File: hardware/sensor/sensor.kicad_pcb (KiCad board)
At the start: 2 copper layers, 64 x 32 mm, 35 parts, among them IC1 ATTINY202-SSN, IC2 Si4012-C1001GTR, IC3 TPS3839L30DBZR, J1 M20-9770342

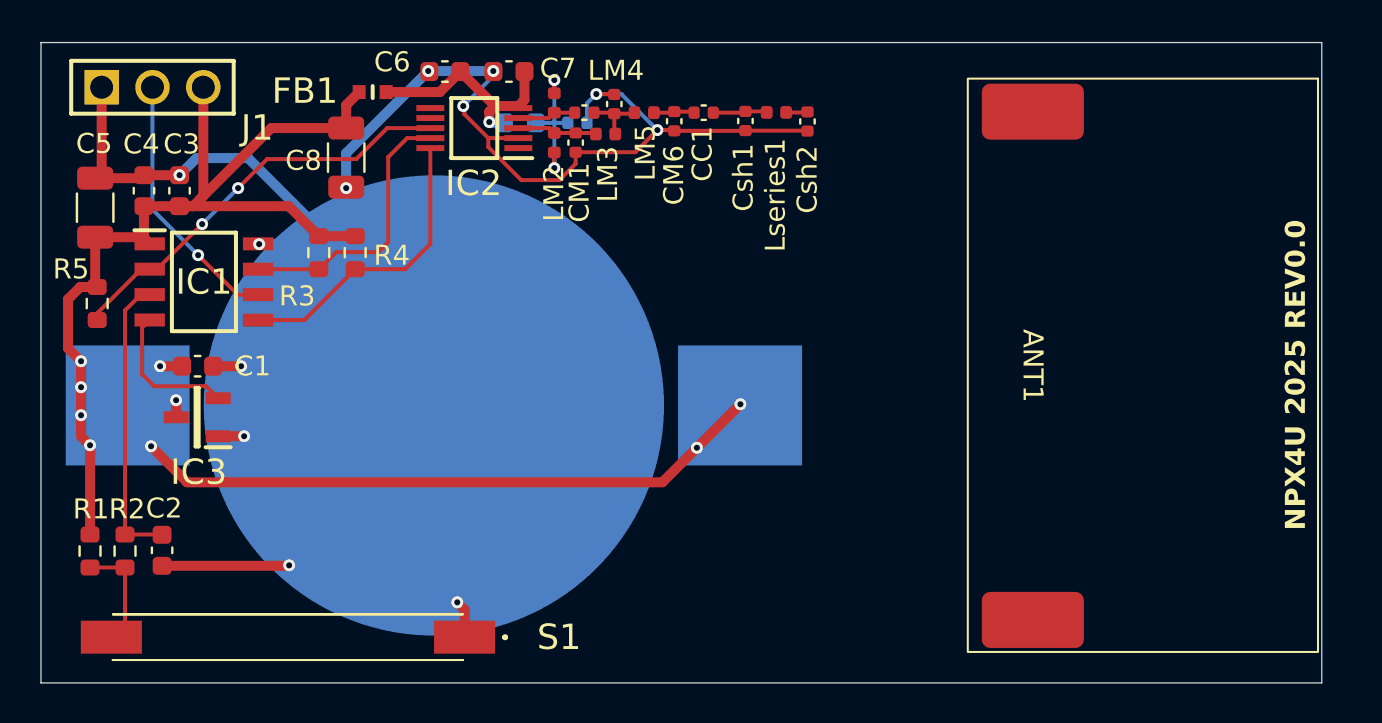
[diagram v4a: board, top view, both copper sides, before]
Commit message: EG-22 All connections, including antenna path and ground planes. Only vias are missing between groud planes.
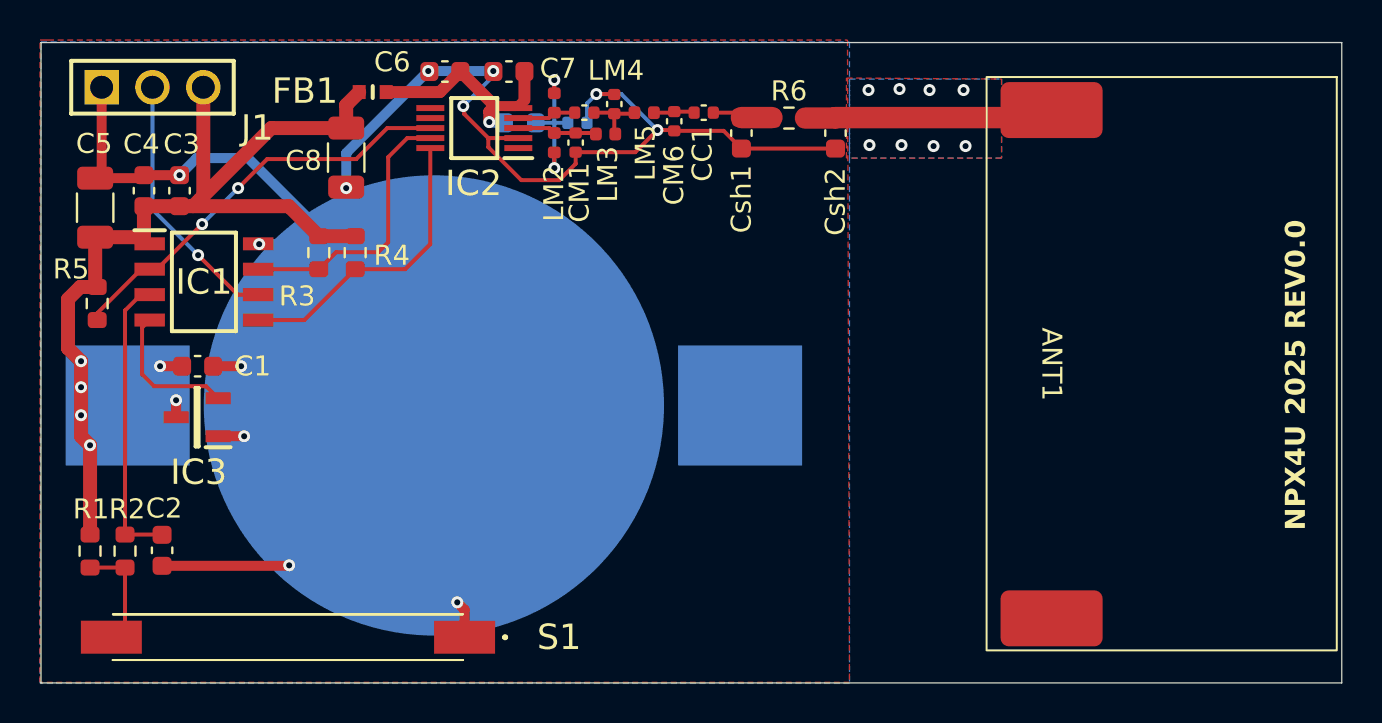
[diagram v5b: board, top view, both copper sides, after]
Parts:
- removed Lseries1: 15nH, Inductor_SMD:L_0402_1005Metric
- added R6: 0, Resistor_SMD:R_0603_1608Metric, F.Cu at (215.1, 130.9)
- Csh1, Csh2: value 0pF -> NC; footprint Capacitor_SMD:C_0402_1005Metric -> Capacitor_SMD:C_0603_1608Metric
- moved Csh2 1.52 mm to (217.4, 131.7)
- moved ANT1 0.94 mm to (228.2, 143.2)
- moved Csh1 0.64 mm to (212.7, 131.7)
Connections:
- H1 pad 1: 3.0V -> unconnected-(H1-+_1-Pad1)
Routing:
- net 3.0V: track 84.1 -> 52.2 mm, vias 9 -> 6
- net Net-(ANT1-Pad1): track 1.09 -> 12.5 mm
- net GND: track 115.9 -> 117.7 mm, vias 12 -> 20
- added copper zone on B.Cu, net GND
- added copper zone on F.Cu, net GND
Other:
- board size 64 x 32 mm -> 65 x 32 mm

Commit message: EG-22 All vias placed.
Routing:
- net GND: vias 20 -> 123

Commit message: EG-29 MCU changed on schematic.
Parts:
- removed IC1: ATTINY202-SSN, MyParts:SOIC127P600X175-8N
- added IC4: STM8L001J3M3, MyParts:SOIC127P600X175-8N, F.Cu at (166.7, 138.9)
- moved IC3 17.3 mm to (168.3, 148.0)
- moved C1 17.3 mm to (168.3, 145.4)
- moved R3 7.47 mm to (198.9, 139.0)
- moved R4 7.47 mm to (200.8, 138.9)
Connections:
- J1 pad 2: UPDI -> SWIM
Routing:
- net SDN: track 21.3 -> 0.00 mm, vias 2 -> 0
- net SDA: track 15.0 -> 0.00 mm
- net GND: track 117.7 -> 102.8 mm, vias 123 -> 117
- net SCL: track 14.0 -> 0.00 mm
- net WND: track 15.1 -> 1.91 mm
- net UPDI: track 13.2 -> 0.00 mm, vias 1 -> 0
- net 3.0V: track 52.2 -> 40.9 mm, vias 6 -> 4
- net LOW_BAT: track 7.16 -> 0.00 mm

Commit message: EG-29 MCU changed on PCB and antenna distance fixed.
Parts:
- moved IC1 18.1 mm to (184.8, 139.9)
- moved C1 17.2 mm to (185.5, 144.7)
- moved IC3 17.2 mm to (185.5, 147.2)
- moved R4 10.1 mm to (190.7, 137.6)
- moved R3 10.1 mm to (188.9, 137.6)
- moved ANT1 2.90 mm to (231.1, 143.2)
- renumbered IC4 to IC1
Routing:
- net GND: track 102.8 -> 133.1 mm, vias 117 -> 126
- net SDN: track 0.00 -> 24.6 mm, vias 0 -> 2
- net SDA: track 0.00 -> 21.4 mm
- net SCL: track 0.00 -> 18.6 mm
- net WND: track 1.91 -> 15.9 mm
- net SWIM: track 0.00 -> 10.7 mm, vias 0 -> 1
- net 3.0V: track 40.9 -> 48.3 mm, vias 4 -> 6
- net LOW_BAT: track 0.00 -> 7.01 mm
- net Net-(ANT1-Pad1): track 12.5 -> 15.4 mm
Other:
- board size 65 x 32 mm -> 68 x 32 mm
